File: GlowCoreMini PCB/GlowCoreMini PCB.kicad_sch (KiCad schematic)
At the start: 62 parts, among them P1 Solder_Pad, P10 Solder_Pad, P11 Solder_Pad, P12 Solder_Pad, P13 Solder_Pad, P14 Solder_Pad, P2 Solder_Pad, P3 Solder_Pad, P4 Solder_Pad, P5 Solder_Pad, P6 Solder_Pad, P7 Solder_Pad, P8 Solder_Pad, P9 Solder_Pad, SW1 TS24CA, SW2 TS24CA, SW3 TS24CA, SW4 TS24CA, U1 ESP32-WROOM-32E, U11 AO3400A, U12 CP2102-GMR, U14 UMH3N, U2 SN74LVC2T45DCUR, U3 MSM261D4030H1CPM, U4 SN74LVC1G373DBVR, U5 AP40P05, U6 SPX3819M5-L-3-3_TR, U7 SS54, U9 SN74LVC1G373DBVR

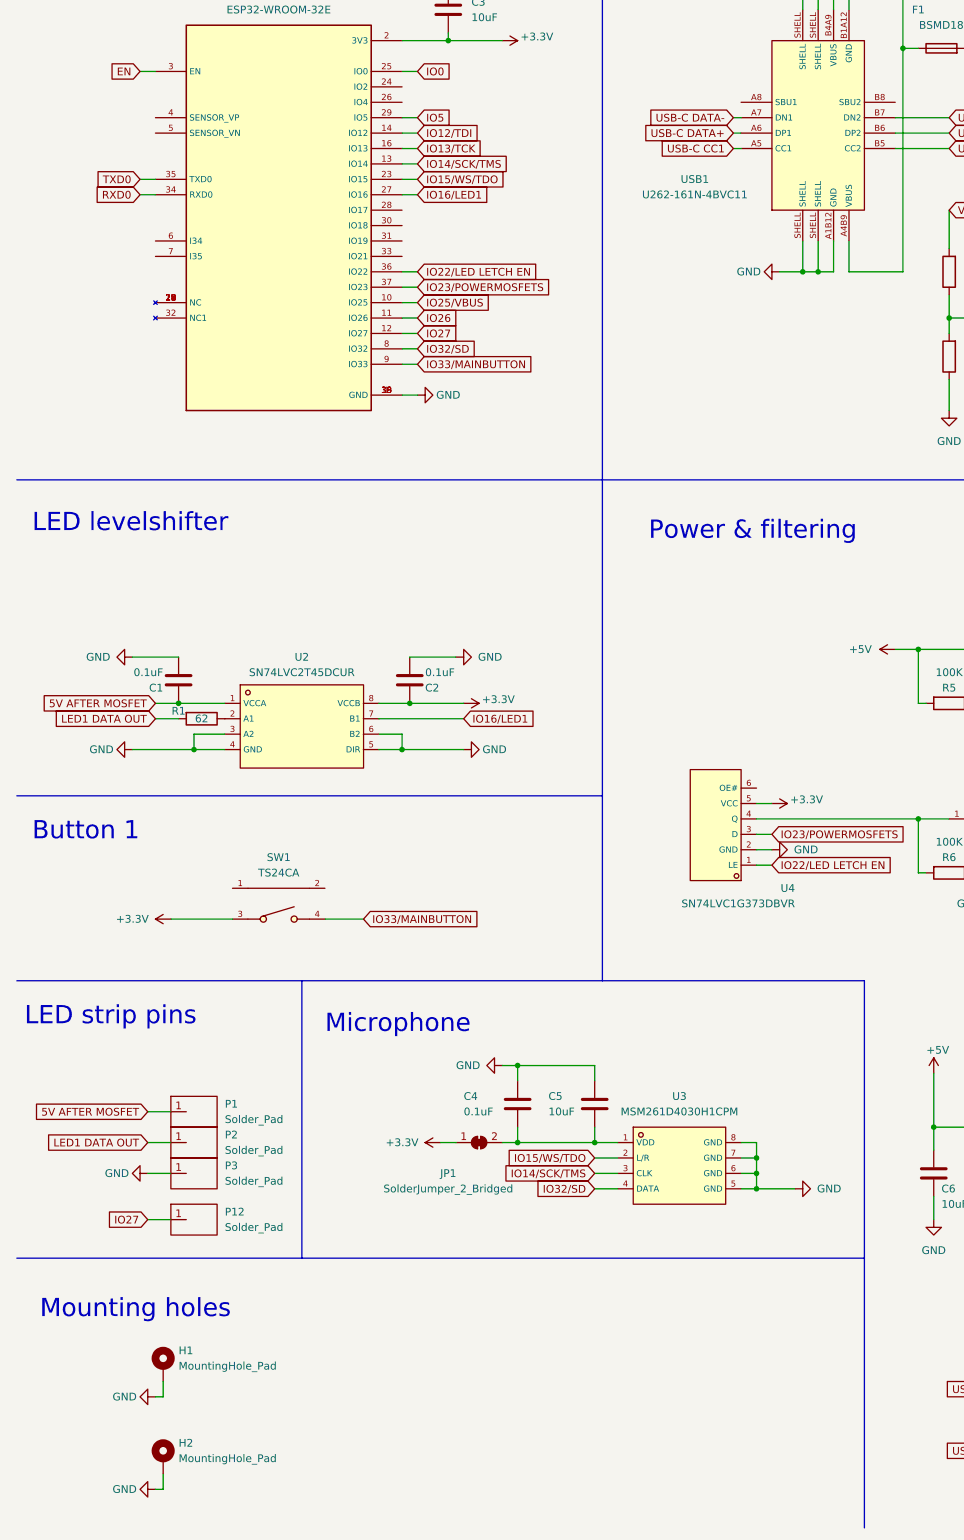
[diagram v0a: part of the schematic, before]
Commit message: added status led
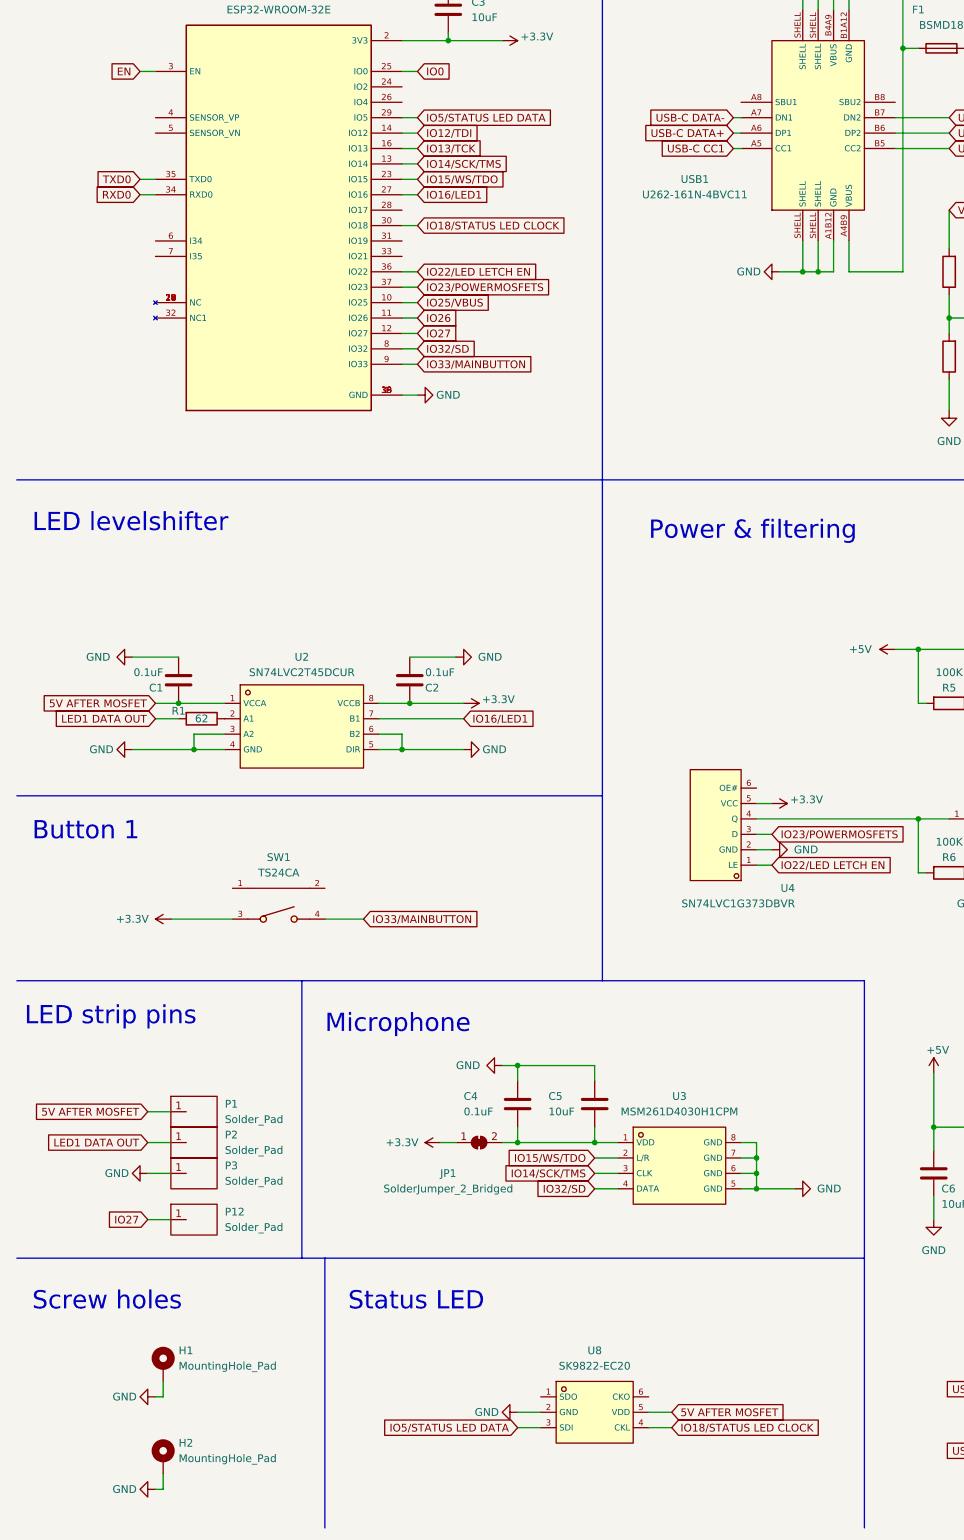
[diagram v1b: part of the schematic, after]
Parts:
- added U8: SK9822-EC20, footprint:LED-SMD_6P-L2.0-W2.0-P0.80-TL, symbol MyParts:SK9822-EC20
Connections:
- net 5V AFTER MOSFET: now also U8.5 (VDD)
- net GND: now also U8.2 (GND)
- net IO18/STATUS LED CLOCK: now reaches U1.30 (IO18)
- net IO18/STATUS LED CLOCK: now also U8.4 (CKL)
- net IO5 renamed IO5/STATUS LED DATA
- net IO5/STATUS LED DATA: now also U8.3 (SDI)
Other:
- note added: "Screw holes"
- note added: "Status LED"
- note removed: "Mounting holes"
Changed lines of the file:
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@@
     (stroke (width 0) (type default) (color 0 0 0 0))
   )
+  (wire (pts (xy 116.84 267.97) (xy 120.65 267.97))
+    (stroke (width 0) (type default) (color 0 0 0 0))
+  )
   (wire (pts (xy 218.44 31.75) (xy 215.9 31.75))
     (stroke (width 0) (type default) (color 0 0 0 0))
@@
     (stroke (width 0) (type default) (color 0 0 0 0))
   )
+  (wire (pts (xy 76.2 69.85) (xy 78.74 69.85))
+    (stroke (width 0) (type default) (color 0 0 0 0))
+  )
   (wire (pts (xy 163.83 209.55) (xy 163.83 218.44))
     (stroke (width 0) (type default) (color 0 0 0 0))
@@
     (stroke (width 0) (type default) (color 0 0 0 0))
   )
+  (wire (pts (xy 95.25 267.97) (xy 99.06 267.97))
+    (stroke (width 0) (type default) (color 0 0 0 0))
+  )
   (wire (pts (xy 370.84 228.6) (xy 370.84 234.95))
     (stroke (width 0) (type default) (color 0 0 0 0))
@@
     (stroke (width 0) (type default) (color 0 0 0 0))
   )
+  (polyline (pts (xy 63.5 240.03) (xy 63.5 284.48))
+    (stroke (width 0) (type default) (color 0 0 0 0))
+  )
   (wire (pts (xy 262.89 76.2) (xy 262.89 50.8))
     (stroke (width 0) (type default) (color 0 0 0 0))
@@
     (stroke (width 0) (type default) (color 0 0 0 0))
   )
+  (wire (pts (xy 95.25 265.43) (xy 99.06 265.43))
+    (stroke (width 0) (type default) (color 0 0 0 0))
+  )
   (wire (pts (xy 158.75 30.48) (xy 158.75 40.64))
     (stroke (width 0) (type default) (color 0 0 0 0))
@@
     (stroke (width 0) (type default) (color 0 0 0 0))
   )
+  (wire (pts (xy 116.84 265.43) (xy 120.65 265.43))
+    (stroke (width 0) (type default) (color 0 0 0 0))
+  )
   (wire (pts (xy 351.79 63.5) (xy 356.87 63.5))
     (stroke (width 0) (type default) (color 0 0 0 0))
@@
     (effects (font (size 3 3)) (justify left bottom))
   )
-  (text "Mounting holes" (at 16.51 250.19 0)
+  (text "Screw holes" (at 15.24 248.92 0)
     (effects (font (size 3 3)) (justify left bottom))
   )
@@
     (effects (font (size 3 3)) (justify left bottom))
   )
+  (text "Status LED" (at 67.31 248.92 0)
+    (effects (font (size 3 3)) (justify left bottom))
+  )
   (text "Power & filtering" (at 116.84 121.92 0)
     (effects (font (size 3 3)) (justify left bottom))
@@
     )
   )
+  (global_label "IO18{slash}STATUS LED CLOCK" (shape input) (at 78.74 69.85 0) (fields_autoplaced)
+    (effects (font (size 1.27 1.27)) (justify left))
+    (property "Intersheet References" "${INTERSHEET_REFS}" (id 0) (at 105.1621 69.7706 0)
+      (effects (font (size 1.27 1.27)) (justify left) hide)
+    )
+  )
   (global_label "IO14{slash}SCK/TMS" (shape input) (at 351.79 53.34 180) (fields_autoplaced)
     (effects (font (size 1.27 1.27)) (justify right))
@@
     )
   )
+  (global_label "IO18{slash}STATUS LED CLOCK" (shape input) (at 120.65 267.97 0) (fields_autoplaced)
+    (effects (font (size 1.27 1.27)) (justify left))
+    (property "Intersheet References" "${INTERSHEET_REFS}" (id 0) (at 147.0721 267.8906 0)
+      (effects (font (size 1.27 1.27)) (justify left) hide)
+    )
+  )
   (global_label "USB-C DATA+" (shape input) (at 166.37 54.61 0) (fields_autoplaced)
     (effects (font (size 1.27 1.27)) (justify left))
@@
     )
   )
+  (global_label "5V AFTER MOSFET" (shape input) (at 120.65 265.43 0) (fields_autoplaced)
+    (effects (font (size 1.27 1.27)) (justify left))
+    (property "Intersheet References" "${INTERSHEET_REFS}" (id 0) (at 129.9574 265.3506 0)
+      (effects (font (size 1.27 1.27)) (justify left) hide)
+    )
+  )
   (global_label "VBUS" (shape input) (at 166.37 67.31 0) (fields_autoplaced)
     (effects (font (size 1.27 1.27)) (justify left))
@@
     )
   )
+  (global_label "IO5{slash}STATUS LED DATA" (shape input) (at 95.25 267.97 180) (fields_autoplaced)
+    (effects (font (size 1.27 1.27)) (justify right))
+    (property "Intersheet References" "${INTERSHEET_REFS}" (id 0) (at 71.7912 268.0494 0)
+      (effects (font (size 1.27 1.27)) (justify right) hide)
+    )
+  )
   (global_label "LED1 DATA OUT" (shape input) (at 35.56 151.13 180) (fields_autoplaced)
     (effects (font (size 1.27 1.27)) (justify right))
@@
     )
   )
-  (global_label "IO5" (shape input) (at 78.74 52.07 0) (fields_autoplaced)
+  (global_label "IO5{slash}STATUS LED DATA" (shape input) (at 78.74 52.07 0) (fields_autoplaced)
     (effects (font (size 1.27 1.27)) (justify left))
-    (property "Intersheet References" "${INTERSHEET_REFS}" (id 0) (at 84.2979 51.9906 0)
+    (property "Intersheet References" "${INTERSHEET_REFS}" (id 0) (at 102.1988 51.9906 0)
       (effects (font (size 1.27 1.27)) (justify left) hide)
     )
@@
     (pin "1")
   )
+  (symbol (lib_id "MyParts:SK9822-EC20") (at 101.6 255.27 0) (unit 1)
+    (in_bom yes) (on_board yes) (fields_autoplaced)
+    (property "Reference" "U8" (id 0) (at 107.95 255.27 0))
+    (property "Value" "SK9822-EC20" (id 1) (at 107.95 257.81 0))
+    (property "Footprint" "footprint:LED-SMD_6P-L2.0-W2.0-P0.80-TL" (id 2) (at 101.6 265.43 0)
+      (effects (font (size 1.27 1.27) italic) hide)
+    )
+    (property "Datasheet" "https://cn.bing.com/search?q=datasheet： APA102-2020" (id 3) (at 99.314 255.143 0)
+      (effects (font (size 1.27 1.27)) (justify left) hide)
+    )
+    (property "LCSC" "C2909059" (id 4) (at 101.6 255.27 0)
+      (effects (font (size 1.27 1.27)) hide)
+    )
+    (pin "1")
+    (pin "2")
+    (pin "3")
+    (pin "4")
+    (pin "5")
+    (pin "6")
+  )
   (symbol (lib_id "power:+3.3V") (at 218.44 36.83 270) (unit 1)
     (in_bom yes) (on_board yes)
@@
     (pin "1")
   )
+  (symbol (lib_id "power:GND") (at 95.25 265.43 270) (unit 1)
+    (in_bom yes) (on_board yes)
+    (property "Reference" "#PWR0141" (id 0) (at 88.9 265.43 0)
+      (effects (font (size 1.27 1.27)) hide)
+    )
+    (property "Value" "GND" (id 1) (at 90.17 265.43 90))
+    (property "Footprint" "" (id 2) (at 95.25 265.43 0)
+      (effects (font (size 1.27 1.27)) hide)
+    )
+    (property "Datasheet" "" (id 3) (at 95.25 265.43 0)
+      (effects (font (size 1.27 1.27)) hide)
+    )
+    (pin "1")
+  )
   (symbol (lib_id "Device:10uF 0603") (at 204.47 229.87 180) (unit 1)
     (in_bom yes) (on_board yes)
@@
       (reference "#PWR0140") (unit 1) (value "GND") (footprint "")
     )
+    (path "/cb77b880-ef19-4df6-af81-3209f7b1e8df"
+      (reference "#PWR0141") (unit 1) (value "GND") (footprint "")
+    )
     (path "/3beca1f1-aa08-4044-a60f-661c43067895"
       (reference "#PWR0142") (unit 1) (value "GND") (footprint "")
@@
       (reference "U7") (unit 1) (value "SS54") (footprint "footprint:SMA_L4.4-W2.8-LS5.4-RD")
     )
+    (path "/a3a98683-cfa5-40ca-8ebf-a9a87366d9c5"
+      (reference "U8") (unit 1) (value "SK9822-EC20") (footprint "footprint:LED-SMD_6P-L2.0-W2.0-P0.80-TL")
+    )
     (path "/7a913f84-cbc5-4d02-80e5-129cae28a0d9"
